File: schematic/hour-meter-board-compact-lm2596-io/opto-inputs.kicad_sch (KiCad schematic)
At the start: 19 parts, among them J301 DIN1 DIN2 COM, U301 PC817C-S, U302 PC817C-S

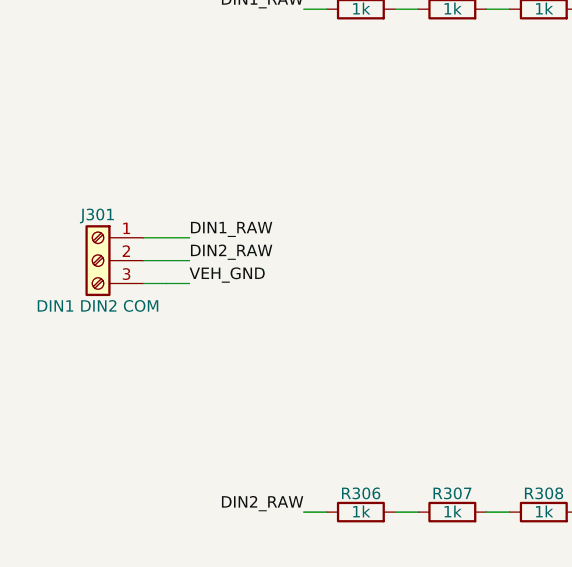
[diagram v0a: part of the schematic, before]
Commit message: fix(pcb): link the I/O board's TP101/TP102 solder pads to their nets
- TP101 (VIN) and TP102 (GND) replace the two-hole TP101: 1.5 mm pads on
  the back, above and below J101. They were placed by hand in the PCB
  editor, so they had no symbol link and no net and could not be routed
- they are now library footprints flipped to the bottom and linked to
  their symbols. A 0.5 mm B.Cu track joins J101 pin 1 to TP101, and TP102
  joins the GND pour solid (its thermal spokes were thinner than the
  pour's minimum)
- pours refilled, so the clearance and solder-mask errors are gone:
  DRC 0 errors, 0 unconnected, 0 parity
- tools-pcb.py: TP101/TP102 placed on the bottom side; `reuse` leaves out
  the LM2596 board's route to its two-hole TP101, which would cross TP102
- includes the board move and the KiCad 10 re-save of the sheets
- production: Gerbers and CPL regenerated, BOM unchanged
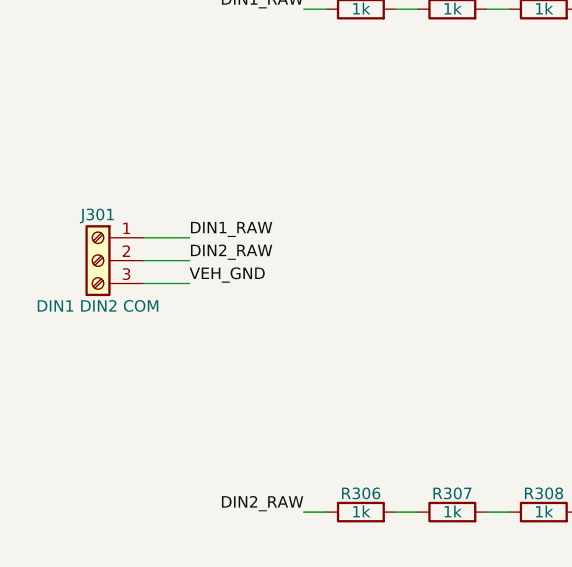
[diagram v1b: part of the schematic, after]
